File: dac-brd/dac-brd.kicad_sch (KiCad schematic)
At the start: 24 parts, among them J1 STK1, J2 I2C/1Wire, J3 UART, J4 STK2, J5 STK3, J6 STK4, U1 REF5020ID, U2 DAC5578xPW, U3 DAC5578xPW

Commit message: Updated all boards for production
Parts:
- removed J4: STK2, Connector_Molex:Molex_PicoBlade_53261-0971_1x09-1MP_P1.25mm_Horizontal, symbol Connector_Generic_MountingPin:Conn_01x09_MountingPin
- removed J5: STK3, Connector_Molex:Molex_PicoBlade_53261-0971_1x09-1MP_P1.25mm_Horizontal, symbol Connector_Generic_MountingPin:Conn_01x09_MountingPin
- removed J6: STK4, Connector_Molex:Molex_PicoBlade_53261-0971_1x09-1MP_P1.25mm_Horizontal, symbol Connector_Generic_MountingPin:Conn_01x09_MountingPin
- added H5, H6: ~, MountingHole:MountingHole_2.7mm_M2.5_Pad_Via, symbol Mechanical:MountingHole_Pad
- added J4: STK2, Connector_Molex:Molex_PicoBlade_53261-1071_1x10-1MP_P1.25mm_Horizontal, symbol Connector_Generic_MountingPin:Conn_01x10_MountingPin
- added J5: STK3, Connector_Molex:Molex_PicoBlade_53261-1071_1x10-1MP_P1.25mm_Horizontal, symbol Connector_Generic_MountingPin:Conn_01x10_MountingPin
- added J6: STK4, Connector_Molex:Molex_PicoBlade_53261-1071_1x10-1MP_P1.25mm_Horizontal, symbol Connector_Generic_MountingPin:Conn_01x10_MountingPin
- added J7: LED, Connector_Molex:Molex_PicoBlade_53398-0271_1x02-1MP_P1.25mm_Vertical, symbol Connector_Generic_MountingPin:Conn_01x02_MountingPin
- H1, H2, H3, H4: value MountingHole_Pad -> ~
- J3: renamed from J1; footprint Connector_Molex:Molex_PicoBlade_53261-0971_1x09-1MP_P1.25mm_Horizontal -> Connector_Molex:Molex_PicoBlade_53261-1071_1x10-1MP_P1.25mm_Horizontal; symbol Connector_Generic_MountingPin:Conn_01x09_MountingPin -> Connector_Generic_MountingPin:Conn_01x10_MountingPin
- renumbered J2 to J1, J3 to J2
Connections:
- net +3V3: now also J4.1 (Pin_1), J4.9 (Pin_9), J5.1 (Pin_1), J6.1 (Pin_1)
- net EN: now also J4.2 (Pin_2), J5.2 (Pin_2), J6.2 (Pin_2)
- net GND: now also J3.10 (Pin_10), H5.1, H6.1, J4.10 (Pin_10), J4.MP (MountPin), J5.10 (Pin_10), J5.MP (MountPin), J6.10 (Pin_10), J6.MP (MountPin), J7.2 (Pin_2), J7.MP (MountPin)
- net OUT_0: now also J4.6 (Pin_6)
- net OUT_10: now also J6.5 (Pin_5)
- net OUT_11: now also J5.5 (Pin_5)
- net OUT_12: now also J6.4 (Pin_4)
- net OUT_13: now also J5.4 (Pin_4)
- net OUT_14: now also J6.3 (Pin_3)
- net OUT_15: now also J5.3 (Pin_3)
- net OUT_2: now also J4.5 (Pin_5)
- net OUT_4: now also J4.4 (Pin_4)
- net OUT_6: now also J4.3 (Pin_3)
- net OUT_8: now also J6.6 (Pin_6)
- net OUT_9: now also J5.6 (Pin_6)
- net SCL1: now also J3.8 (Pin_8), J4.8 (Pin_8), J5.8 (Pin_8), J6.8 (Pin_8), J6.9 (Pin_9); no longer J3.7 (Pin_7)
- net SDA1: now also J3.7 (Pin_7), J4.7 (Pin_7), J5.7 (Pin_7), J5.9 (Pin_9), J6.7 (Pin_7); no longer J3.8 (Pin_8)
- net LED: now reaches A1.16 (GPIO12)
- net LED: now also J7.1 (Pin_1)
- no-connect marks 23 -> 22

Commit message: Updated dac-brd connectors to vertical
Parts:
- J3, J4, J5, J6: footprint Connector_Molex:Molex_PicoBlade_53261-1071_1x10-1MP_P1.25mm_Horizontal -> Connector_Molex:Molex_PicoBlade_53398-1071_1x10-1MP_P1.25mm_Vertical
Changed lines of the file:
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@@
 			)
 		)
-		(property "Footprint" "Connector_Molex:Molex_PicoBlade_53261-1071_1x10-1MP_P1.25mm_Horizontal"
+		(property "Footprint" "Connector_Molex:Molex_PicoBlade_53398-1071_1x10-1MP_P1.25mm_Vertical"
 			(at 31.75 33.02 0)
 			(effects
@@
 			)
 		)
-		(property "Footprint" "Connector_Molex:Molex_PicoBlade_53261-1071_1x10-1MP_P1.25mm_Horizontal"
+		(property "Footprint" "Connector_Molex:Molex_PicoBlade_53398-1071_1x10-1MP_P1.25mm_Vertical"
 			(at 31.75 170.18 0)
 			(effects
@@
 			)
 		)
-		(property "Footprint" "Connector_Molex:Molex_PicoBlade_53261-1071_1x10-1MP_P1.25mm_Horizontal"
+		(property "Footprint" "Connector_Molex:Molex_PicoBlade_53398-1071_1x10-1MP_P1.25mm_Vertical"
 			(at 31.75 78.74 0)
 			(effects
@@
 			)
 		)
-		(property "Footprint" "Connector_Molex:Molex_PicoBlade_53261-1071_1x10-1MP_P1.25mm_Horizontal"
+		(property "Footprint" "Connector_Molex:Molex_PicoBlade_53398-1071_1x10-1MP_P1.25mm_Vertical"
 			(at 31.75 123.19 0)
 			(effects

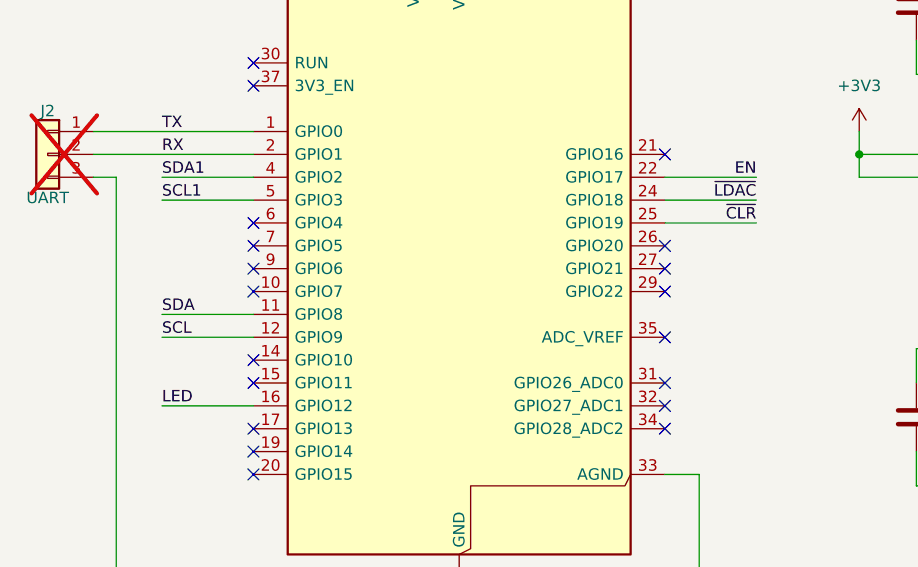
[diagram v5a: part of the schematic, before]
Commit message: Indicate using rp2350a. Re-wire I2C0 connections on DAC board for easier layout
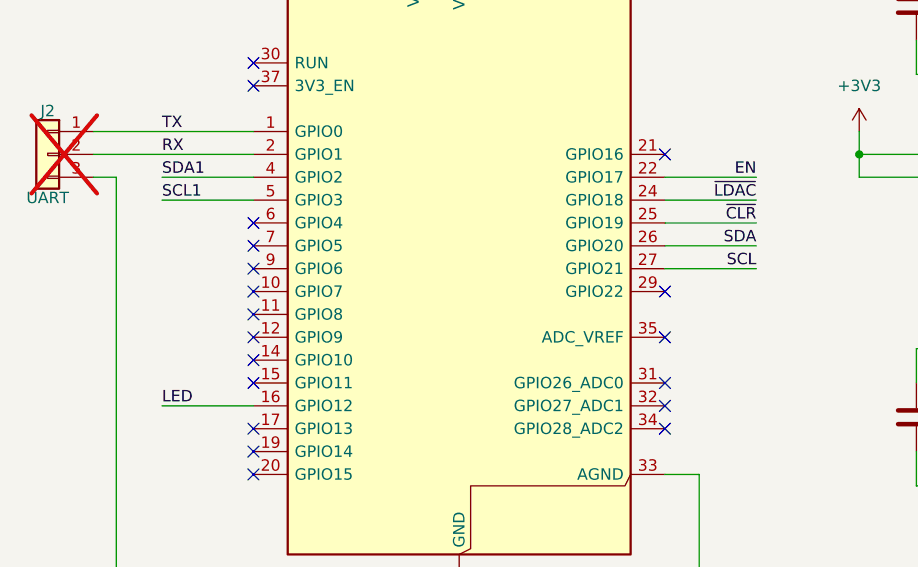
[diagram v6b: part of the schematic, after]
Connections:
- net SCL: now also A1.27 (GPIO21); no longer A1.12 (GPIO9)
- net SDA: now also A1.26 (GPIO20); no longer A1.11 (GPIO8)
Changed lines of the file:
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@@
 	)
 	(no_connect
-		(at 170.18 92.71)
+		(at 124.46 102.87)
 	)
 	(no_connect
@@
 	)
 	(no_connect
+		(at 124.46 100.33)
+	)
+	(no_connect
 		(at 124.46 118.11)
 	)
@@
 	)
 	(no_connect
-		(at 170.18 95.25)
-	)
-	(no_connect
 		(at 238.76 147.32)
 	)
@@
 	(wire
 		(pts
-			(xy 114.3 102.87) (xy 124.46 102.87)
+			(xy 180.34 95.25) (xy 170.18 95.25)
 		)
 		(stroke
@@
 	(wire
 		(pts
-			(xy 114.3 100.33) (xy 124.46 100.33)
+			(xy 180.34 92.71) (xy 170.18 92.71)
 		)
 		(stroke
@@
 	)
 	(label "SDA"
-		(at 114.3 100.33 0)
-		(effects
-			(font
-				(size 1.27 1.27)
-			)
-			(justify left bottom)
+		(at 180.34 92.71 180)
+		(effects
+			(font
+				(size 1.27 1.27)
+			)
+			(justify right bottom)
 		)
 	)
@@
 	)
 	(label "SCL"
-		(at 114.3 102.87 0)
-		(effects
-			(font
-				(size 1.27 1.27)
-			)
-			(justify left bottom)
-		)
-	)
+		(at 180.34 95.25 180)
+		(effects
+			(font
+				(size 1.27 1.27)
+			)
+			(justify right bottom)
+		)
+	)

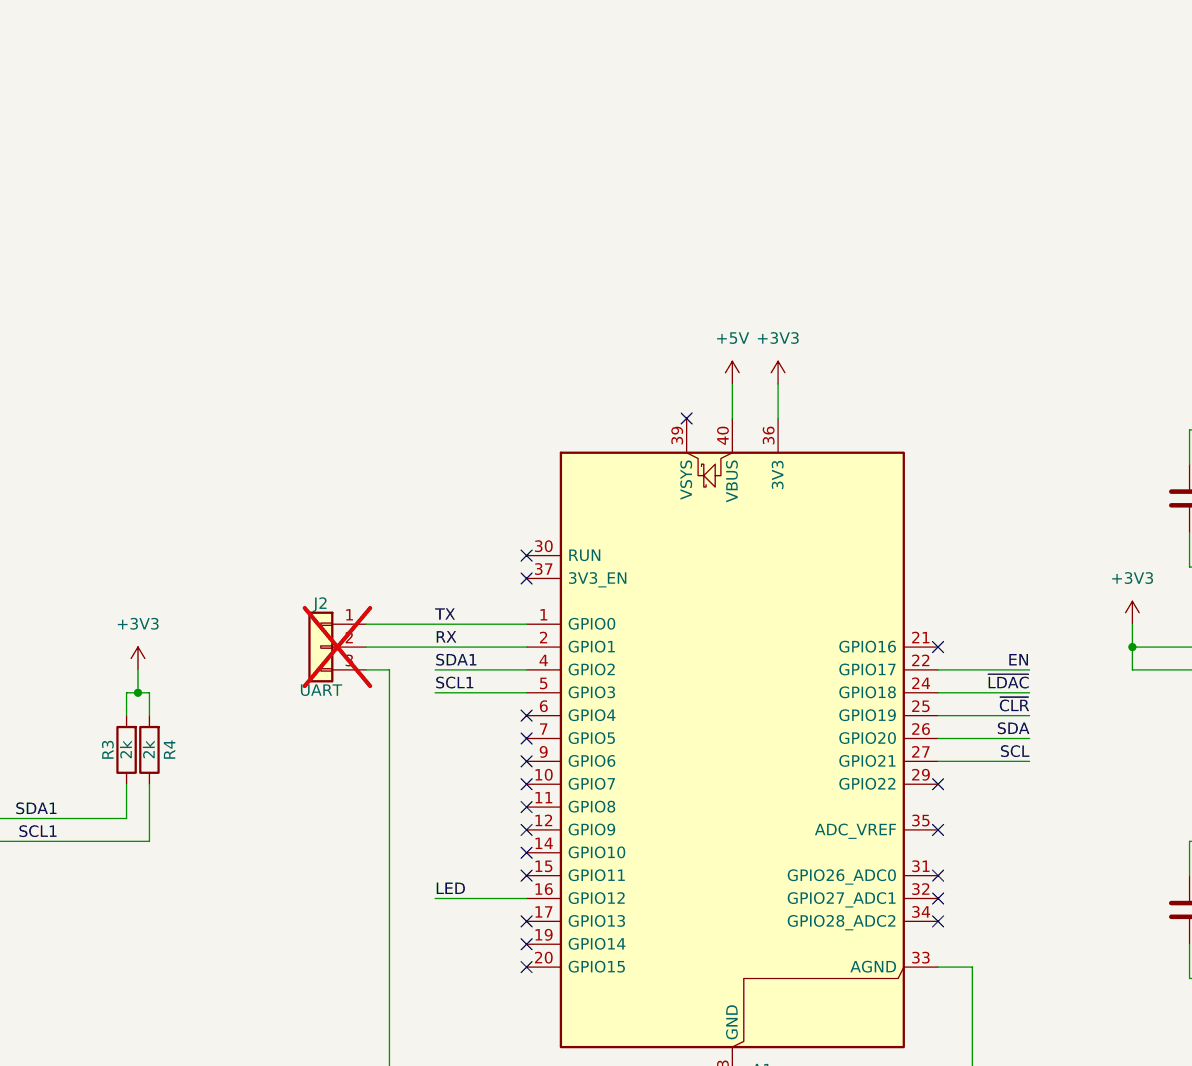
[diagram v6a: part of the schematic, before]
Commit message: Adding power conditioning board
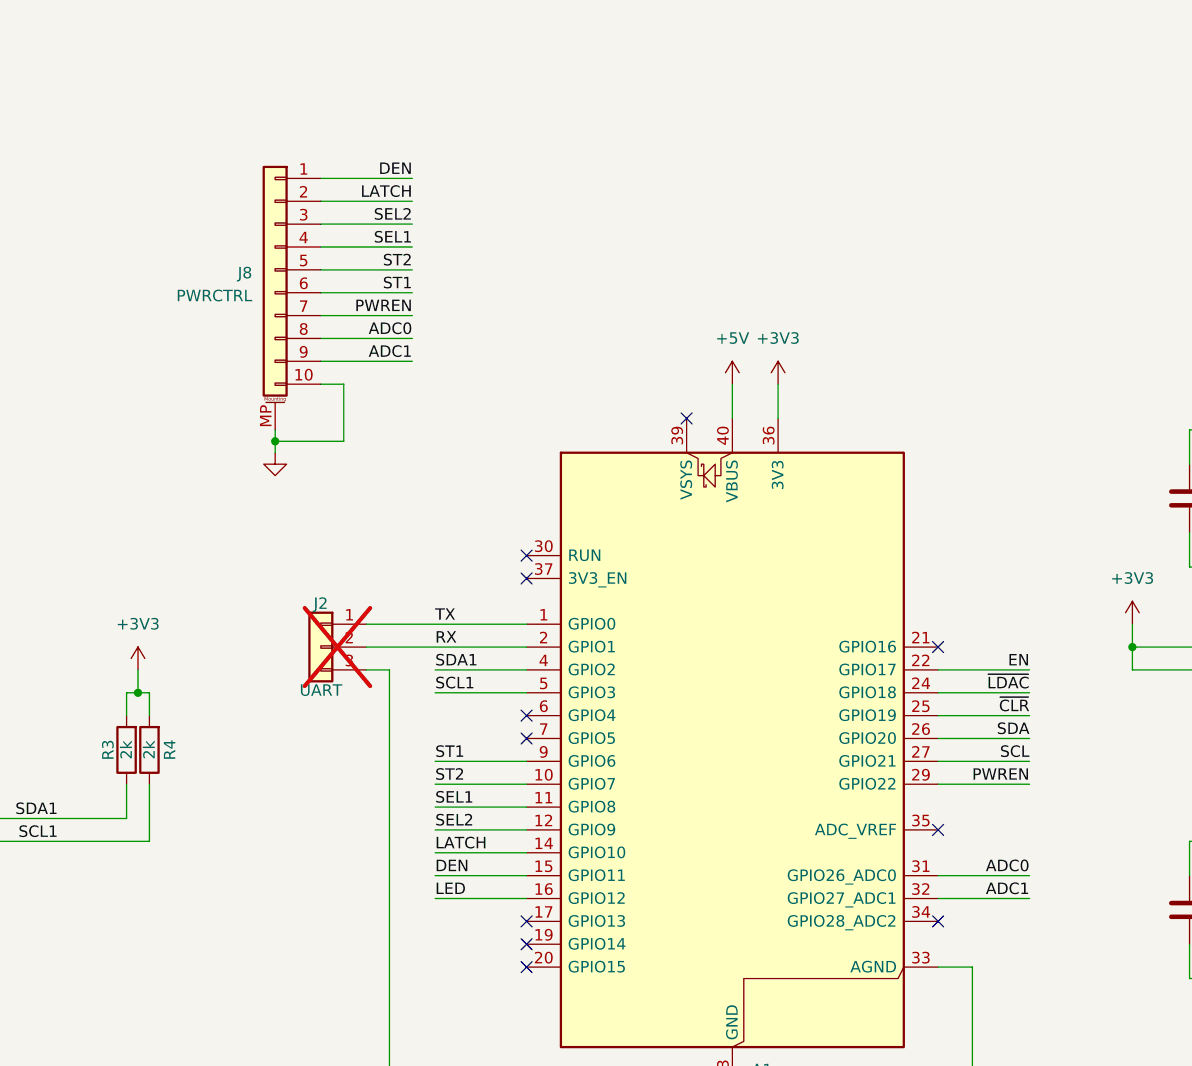
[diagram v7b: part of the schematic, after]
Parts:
- added J8: PWRCTRL, Connector_Molex:Molex_PicoBlade_53261-1071_1x10-1MP_P1.25mm_Horizontal, symbol Connector_Generic_MountingPin:Conn_01x10_MountingPin
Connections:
- net GND: now also J8.10 (Pin_10), J8.MP (MountPin)
- net ST2: now reaches A1.10 (GPIO7)
- net ST2: now also J8.5 (Pin_5)
- net SEL1: now reaches A1.11 (GPIO8)
- net SEL1: now also J8.4 (Pin_4)
- net SEL2: now reaches A1.12 (GPIO9)
- net SEL2: now also J8.3 (Pin_3)
- net LATCH: now reaches A1.14 (GPIO10)
- net LATCH: now also J8.2 (Pin_2)
- net DEN: now reaches A1.15 (GPIO11)
- net DEN: now also J8.1 (Pin_1)
- net PWREN: now reaches A1.29 (GPIO22)
- net PWREN: now also J8.7 (Pin_7)
- net ADC0: now reaches A1.31 (GPIO26_ADC0)
- net ADC0: now also J8.8 (Pin_8)
- net ADC1: now reaches A1.32 (GPIO27_ADC1)
- net ADC1: now also J8.9 (Pin_9)
- net ST1: now reaches A1.9 (GPIO6)
- net ST1: now also J8.6 (Pin_6)
- no-connect marks 22 -> 13
